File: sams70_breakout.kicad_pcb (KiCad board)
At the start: 2 copper layers, 45.2 x 26.5 mm, 32 parts, among them J1 USB_OTG, J2 Conn_01x04, J3 Conn_01x16, J4 Conn_01x16, J5 Conn_01x07, J6 Conn_01x07, U1 ATSAME70J20A-AN, U2 XC6206P332MR, Y1 16MHz

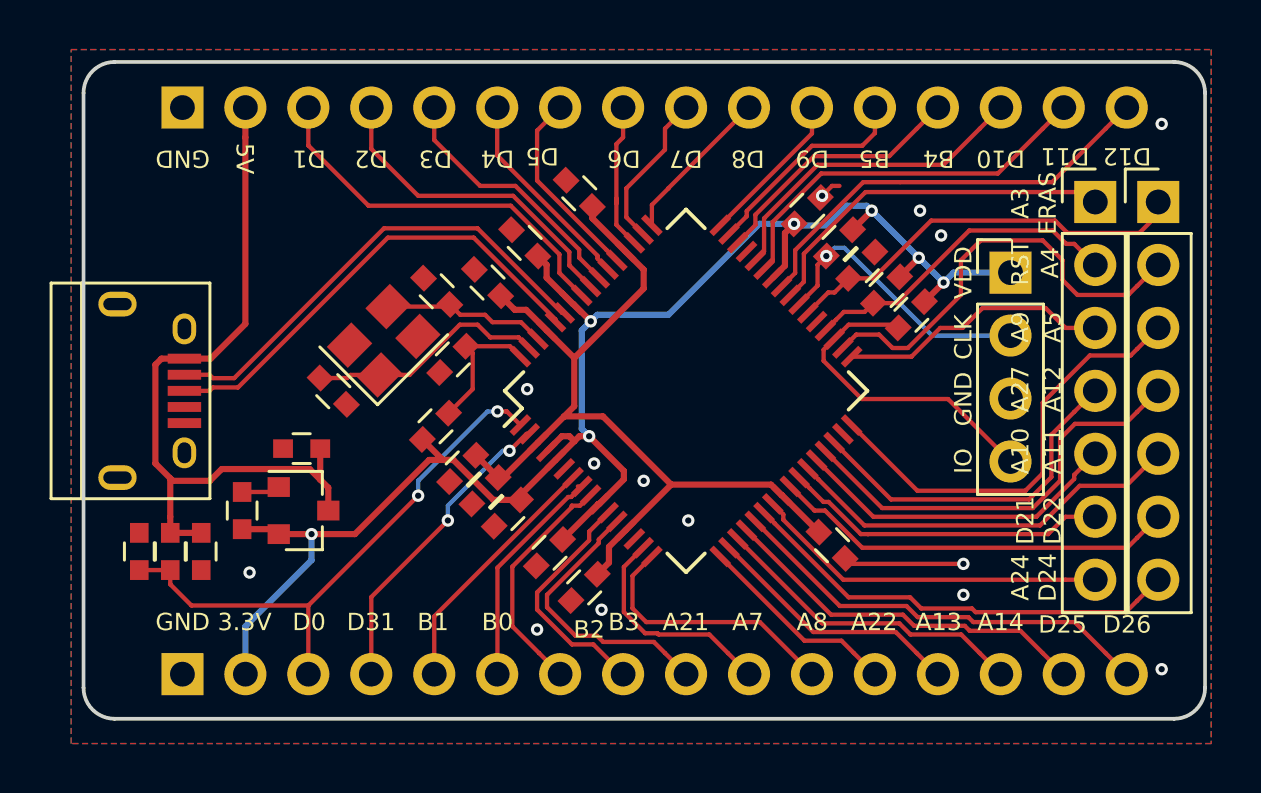
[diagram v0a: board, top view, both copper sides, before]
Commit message: Add PWR LED and update footprints to KiCAD nightly
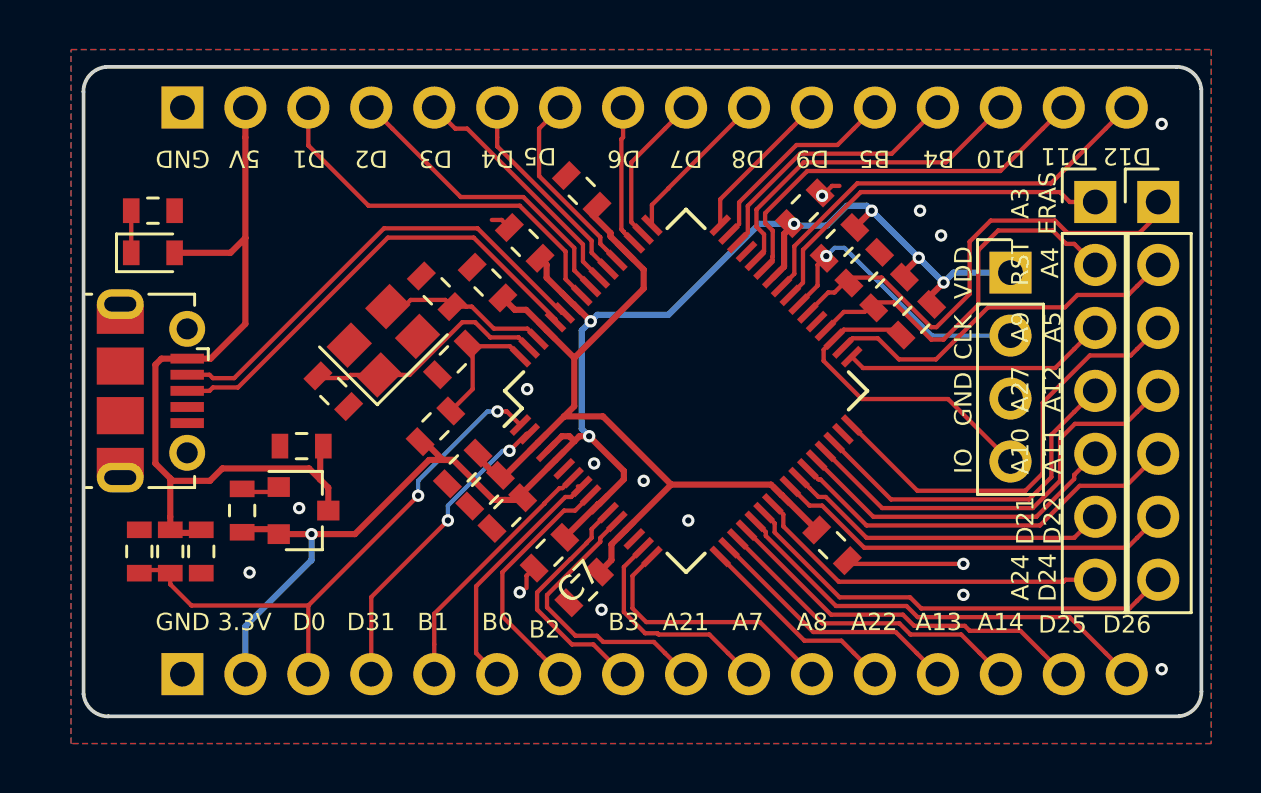
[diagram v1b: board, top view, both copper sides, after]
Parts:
- added D1: PWR, LED_SMD:LED_0603_1608Metric, F.Cu at (109.3, 59.2)
- added R8: 560R, Resistor_SMD:R_0603_1608Metric, F.Cu at (109.3, 57.5)
- C1, C10, C11, C12, C13, C14, C15, C16, C2, C3, C4, C5, C6, C7, C8, C9: footprint Capacitors_SMD:C_0603 -> Capacitor_SMD:C_0603_1608Metric
- J1: footprint Connectors:USB_Micro-B -> Connector_USB:USB_Micro-B_Molex-105017-0001
- J2: footprint Pin_Headers:Pin_Header_Straight_1x04_Pitch2.54mm -> Connector_PinHeader_2.54mm:PinHeader_1x04_P2.54mm_Vertical
- J3, J4: footprint Pin_Headers:Pin_Header_Straight_1x16_Pitch2.54mm -> Connector_PinHeader_2.54mm:PinHeader_1x16_P2.54mm_Vertical
- J5, J6: footprint Pin_Headers:Pin_Header_Straight_1x07_Pitch2.54mm -> Connector_PinHeader_2.54mm:PinHeader_1x07_P2.54mm_Vertical
- R1, R2, R3, R4, R5, R6, R7: footprint Capacitors_SMD:C_0603 -> Resistor_SMD:R_0603_1608Metric
- U1: footprint Housings_QFP:LQFP-64_10x10mm_Pitch0.5mm -> Package_QFP:LQFP-64_10x10mm_P0.5mm
- U2: footprint TO_SOT_Packages_SMD:SOT-23 -> Package_TO_SOT_SMD:SOT-23
- Y1: footprint Crystals:Crystal_SMD_3225-4pin_3.2x2.5mm -> Crystal:Crystal_SMD_3225-4Pin_3.2x2.5mm
- moved R6 0.28 mm to (140.1, 61.9)
- moved C8 0.14 mm to (135.6, 57.4)
- moved C13 0.14 mm to (126.6, 56.7)
- moved R3 0.14 mm to (139.0, 60.8)
- moved R5 0.14 mm to (138.0, 59.8)
- moved C15 0.10 mm to (115.3, 67.0)
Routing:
- net VBUS: track 30.4 -> 33.5 mm
- net /ERASE: track 16.7 -> 19.7 mm
- net /PA4: track 17.7 -> 14.8 mm
- net /RESET: track 13.1 -> 15.8 mm
- net GND: track 7.38 -> 9.15 mm, vias 14 -> 15
- net Net-(D1-Pad1): track 0.00 -> 1.70 mm
- net /PB0: track 9.22 -> 9.99 mm
- net /PD2: track 13.3 -> 12.5 mm
- net /PD11: track 15.7 -> 16.3 mm
- net /PD10: track 13.2 -> 13.9 mm
- net /PD3: track 10.5 -> 9.91 mm
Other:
- board size 45.2 x 26.5 mm -> 45.1 x 26.2 mm
- rule pad_to_mask_clearance: 0.15 -> 0.14
